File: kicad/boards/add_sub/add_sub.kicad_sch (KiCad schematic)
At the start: 0 parts

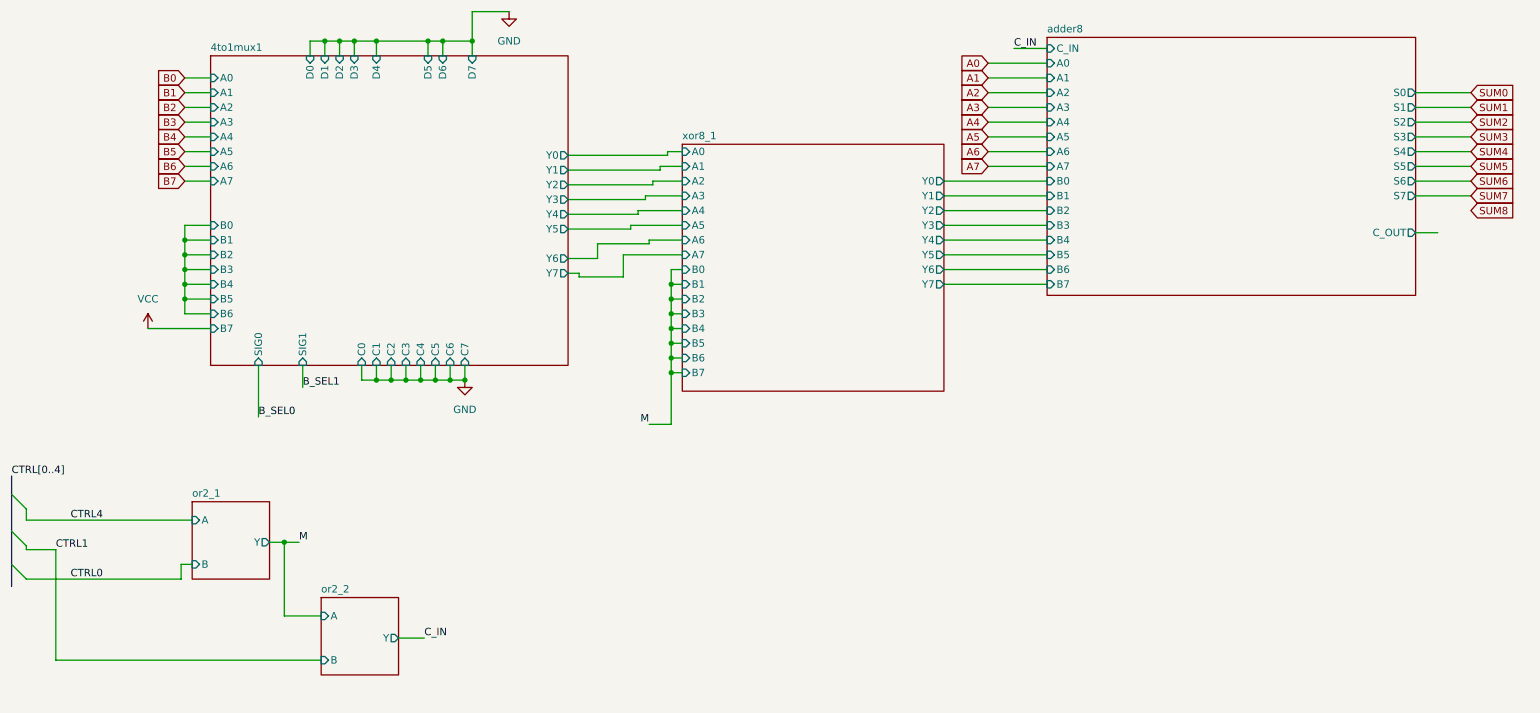
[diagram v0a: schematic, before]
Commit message: feat: complete circuit designs for all ALU components
* Designed all gate modules: AND, OR, NOT, NAND, NOR, XOR (1-bit and 8-bit variants)

* Completed multiplexer hierarchy: 2:1, 4:1, and 8:1 8-bit muxes

* Finalized add_sub board schematic and LED panel designs

* Added new board modules: flags, main_control, main_logic

* Updated Logisim top-level ALU circuit

* Note: KiCad directory path errors to be resolved next (iCloud sync issue), then begin PCB routing
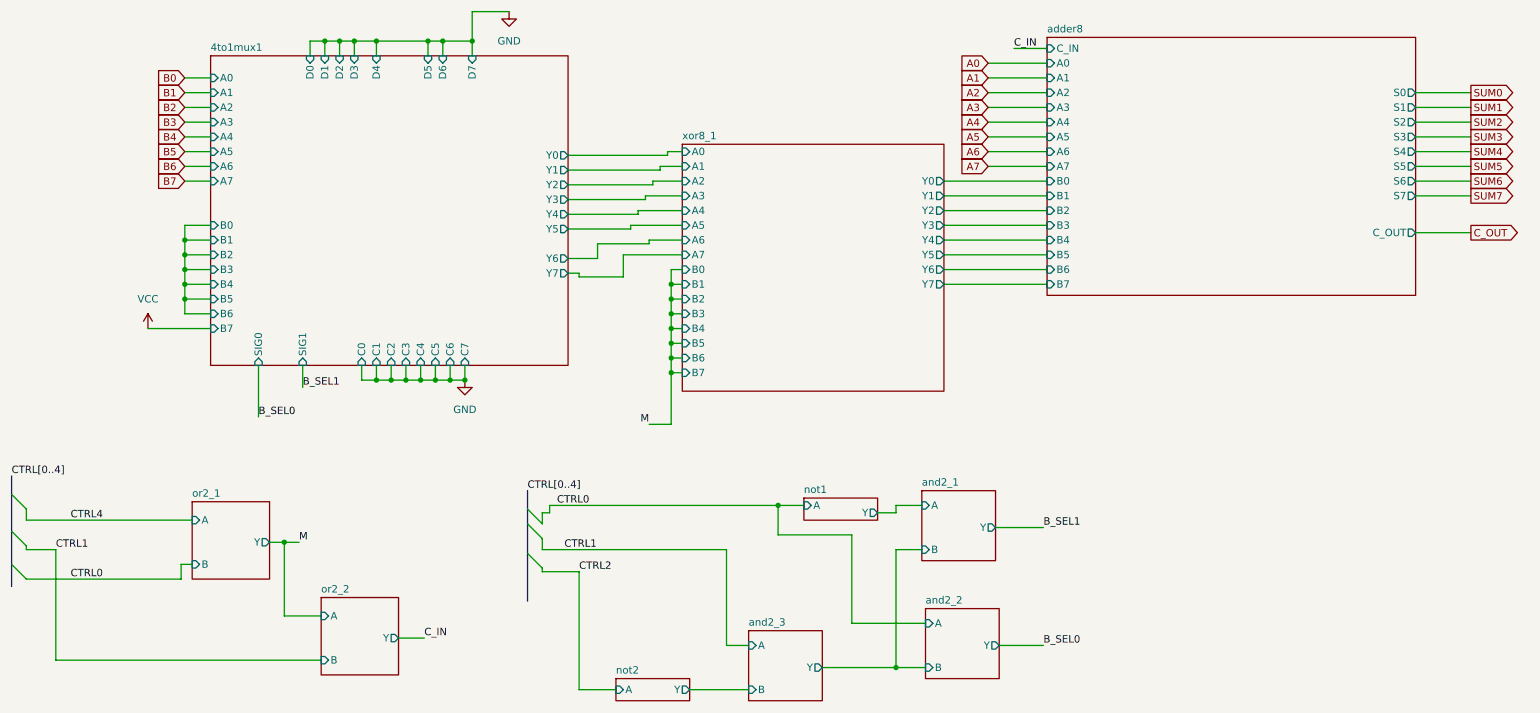
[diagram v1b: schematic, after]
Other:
- added sheet and2_1 (../../modules/gates/gate_and/gate_and_2in/gate_and_2in.kicad_sch)
- added sheet and2_2 (../../modules/gates/gate_and/gate_and_2in/gate_and_2in.kicad_sch)
- added sheet and2_3 (../../modules/gates/gate_and/gate_and_2in/gate_and_2in.kicad_sch)
- added sheet not1 (../../modules/gates/gate_inv/gate_inv_1bit/gate_inv_1bit.kicad_sch)
- added sheet not2 (../../modules/gates/gate_inv/gate_inv_1bit/gate_inv_1bit.kicad_sch)
